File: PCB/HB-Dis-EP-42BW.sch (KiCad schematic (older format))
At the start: 42 parts, among them J1 Reset, J2 FTDI, J3 ISP, J4 ePaper, J5 ePaper_TestPoints, J6 Supply, J7 Conn_GPIO, J8 Config, J9 Conn_I2C, Q1 IRLML6344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

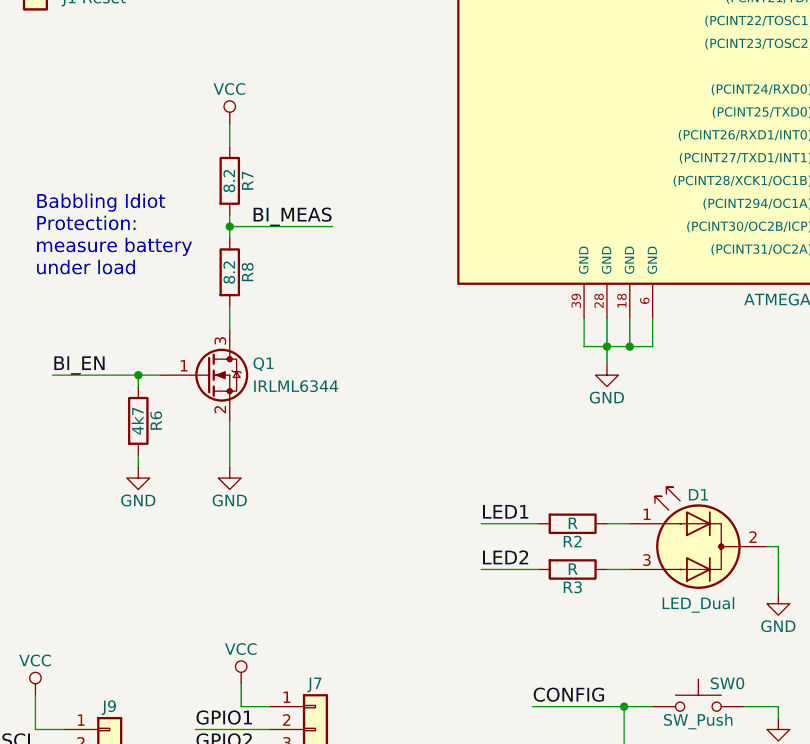
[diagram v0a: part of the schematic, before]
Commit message: update resistor values for BI and LED
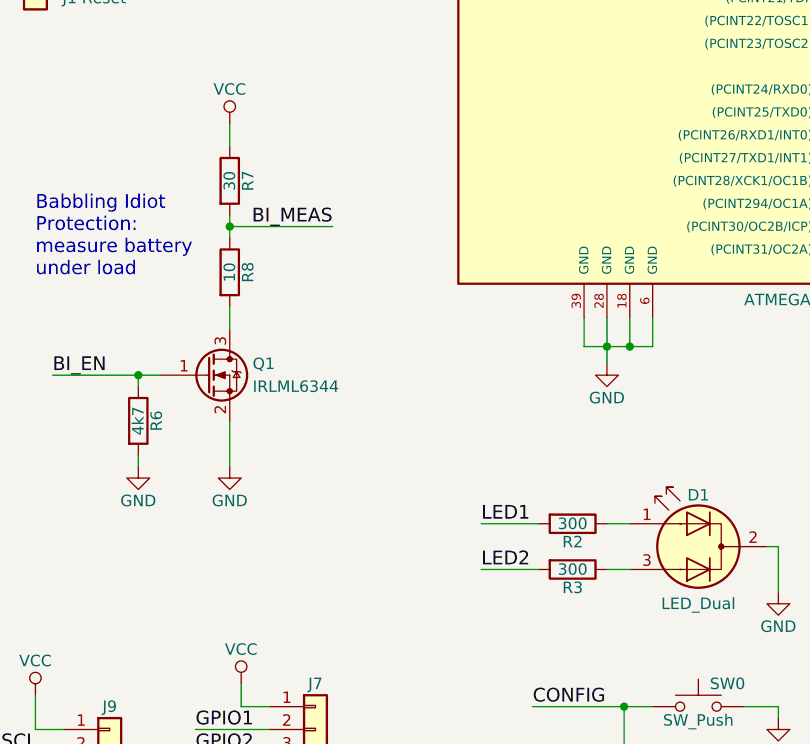
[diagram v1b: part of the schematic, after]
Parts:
- R2, R3: value R -> 300
- R7: value 8.2 -> 30
- R8: value 8.2 -> 10
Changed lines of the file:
@@
 P 4800 6050
 F 0 "R2" V 4880 6050 50  0000 C CNN
-F 1 "R" V 4800 6050 50  0000 C CNN
+F 1 "300" V 4800 6050 50  0000 C CNN
 F 2 "Resistors_SMD:R_0603_HandSoldering" V 4730 6050 50  0001 C CNN
 F 3 "" H 4800 6050 50  0001 C CNN
@@
 P 4800 6250
 F 0 "R3" V 4880 6250 50  0000 C CNN
-F 1 "R" V 4800 6250 50  0000 C CNN
+F 1 "300" V 4800 6250 50  0000 C CNN
 F 2 "Resistors_SMD:R_0603_HandSoldering" V 4730 6250 50  0001 C CNN
 F 3 "" H 4800 6250 50  0001 C CNN
@@
 P 3300 4950
 F 0 "R8" V 3380 4950 50  0000 C CNN
-F 1 "8.2" V 3300 4950 50  0000 C CNN
+F 1 "10" V 3300 4950 50  0000 C CNN
 F 2 "Resistors_SMD:R_0603_HandSoldering" V 3230 4950 50  0001 C CNN
 F 3 "" H 3300 4950 50  0001 C CNN
@@
 P 3300 4550
 F 0 "R7" V 3380 4550 50  0000 C CNN
-F 1 "8.2" V 3300 4550 50  0000 C CNN
+F 1 "30" V 3300 4550 50  0000 C CNN
 F 2 "Resistors_SMD:R_0603_HandSoldering" V 3230 4550 50  0001 C CNN
 F 3 "" H 3300 4550 50  0001 C CNN
